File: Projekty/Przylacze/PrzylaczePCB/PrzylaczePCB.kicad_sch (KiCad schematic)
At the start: 46 parts, among them J1 Conn_02x20_Odd_Even, J2 USB_B, J3 Conn_01x06, J4 Conn_02x04_Odd_Even, J5 Screw_Terminal_01x06, Q3 2N7002, Q4 2N3904, Q5 2N3904, Q6 2N7002, SW1 SW_Push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

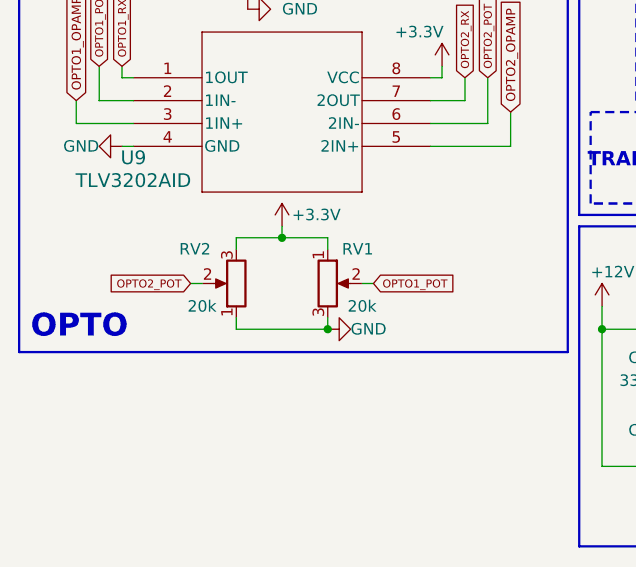
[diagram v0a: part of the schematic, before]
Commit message: Przyłącze - projekt PCB v1.6
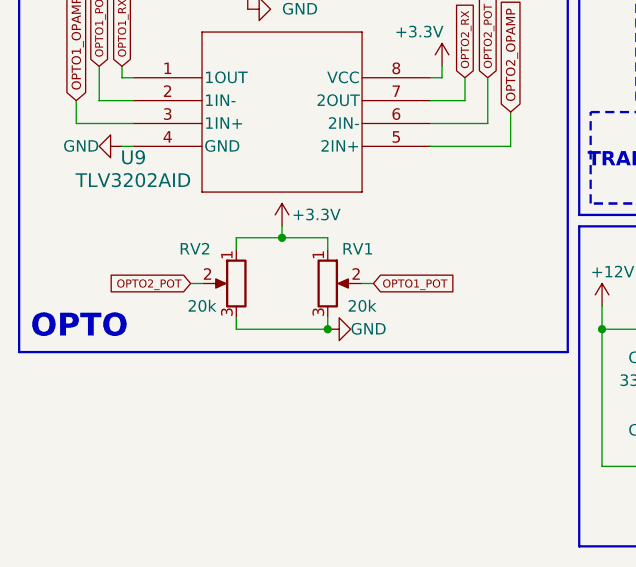
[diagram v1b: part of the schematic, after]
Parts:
- Q4, Q5: footprint Package_TO_SOT_THT:TO-92_Inline -> Package_TO_SOT_THT:TO-92L
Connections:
- net +3.3V: now also RV2.1; no longer RV2.3
- net GND: now also RV2.3; no longer RV2.1
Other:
- moved on the sheet: RV2
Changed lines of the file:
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@@
       (effects (font (size 1.27 1.27)) (justify left))
     )
-    (property "Footprint" "Package_TO_SOT_THT:TO-92_Inline" (at 29.845 55.88 0)
+    (property "Footprint" "Package_TO_SOT_THT:TO-92L" (at 29.845 55.88 0)
       (effects (font (size 1.27 1.27) italic) (justify left) hide)
     )
@@
       (effects (font (size 1.27 1.27)) (justify left))
     )
-    (property "Footprint" "Package_TO_SOT_THT:TO-92_Inline" (at 29.845 26.67 0)
+    (property "Footprint" "Package_TO_SOT_THT:TO-92L" (at 29.845 26.67 0)
       (effects (font (size 1.27 1.27) italic) (justify left) hide)
     )
@@
     )
   )
-  (symbol (lib_id "Device:R_Potentiometer") (at 39.37 149.86 180) (unit 1)
+  (symbol (lib_id "Device:R_Potentiometer") (at 39.37 149.86 0) (mirror y) (unit 1)
     (in_bom yes) (on_board yes) (dnp no)
     (property "Reference" "RV2" (at 33.02 146.05 0)

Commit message: PeCeBe wersja Final Omega Prime Ultimate Fatality
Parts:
- removed Q3, Q6: 2N7002, Package_TO_SOT_SMD:SOT-23, symbol Transistor_FET:2N7002
- added Q3, Q6: BC547, Package_TO_SOT_THT:TO-92_Inline, symbol Transistor_BJT:BC547
- added R35, R36: 600, Resistor_THT:R_Axial_DIN0207_L6.3mm_D2.5mm_P10.16mm_Horizontal, symbol Device:R
- R22, R23: value R -> 1M
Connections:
- net OPTO1_NOT_TX: now also R35.2
- net OPTO2_NOT_TX: now also R36.2
- net at D12.2 (A), R24.2: now also Q6.1 (C)
- net at D10.2 (A), R25.1: now also Q3.1 (C)
- net at R22.2, U6.6 (IN2-): now also Q3.3 (E)
- net at R23.1, U6.2 (IN1-): now also Q6.3 (E)
- new net: Q6.2 (B), R36.1
- new net: Q3.2 (B), R35.1
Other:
- moved on the sheet: D10, D12, Q4, Q5, R22, R23, R24, R25, R26, R34, U6A, U6B
